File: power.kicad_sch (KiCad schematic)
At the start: 53 parts, among them J1 TYPE-C-31-M-12, U1 USBLC6-2SC6, U2 TLV62569DBVR, U3 AP22653W6-7, U4 AP22653W6-7, U5 AP22653W6-7, U6 AP22653W6-7

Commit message: fix: apply schematic review findings (VIO 5V at power-up, push-pull BOOT, input bias, CC ESD)
Co-Authored-By: Claude Opus 5.5 <noreply@anthropic.com>
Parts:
- removed U1: USBLC6-2SC6, Package_TO_SOT_SMD:SOT-23-6, symbol Power_Protection:USBLC6-2SC6
- removed U2: TLV62569DBVR, Package_TO_SOT_SMD:SOT-23-5, symbol Regulator_Switching:TLV62569DBV
- removed U3: AP22653W6-7, Package_TO_SOT_SMD:SOT-23-6, symbol OOTY:AP22653W6
- added U1: TPD4E05U06DQAR, Package_SON:USON-10_2.5x1.0mm_P0.5mm, symbol Power_Protection:TPD4E05U06DQA
- added U2: USBLC6-2SC6, Package_TO_SOT_SMD:SOT-23-6, symbol Power_Protection:USBLC6-2SC6
- added U3: TLV62569DBVR, Package_TO_SOT_SMD:SOT-23-5, symbol Regulator_Switching:TLV62569DBV
- added U7: AP22653W6-7, Package_TO_SOT_SMD:SOT-23-6, symbol OOTY:AP22653W6
- C2: value 10uF/25V -> 100nF/50V; footprint Capacitor_SMD:C_0805_2012Metric -> Capacitor_SMD:C_0402_1005Metric; LCSC C15850 -> C307331; MPN CL21A106KAYNNNE -> CL05B104KB54PNC
- C3: value 100nF/50V -> 10uF/10V; footprint Capacitor_SMD:C_0402_1005Metric -> Capacitor_SMD:C_0603_1608Metric; LCSC C307331 -> C19702; MPN CL05B104KB54PNC -> CL10A106KP8NNNC
- C4: value 10uF/10V -> 100nF/50V; footprint Capacitor_SMD:C_0603_1608Metric -> Capacitor_SMD:C_0402_1005Metric; LCSC C19702 -> C307331; MPN CL10A106KP8NNNC -> CL05B104KB54PNC
- C5: value 100nF/50V -> 6.8pF DNP; LCSC C307331 -> (none); MPN CL05B104KB54PNC -> (none); Manufacturer Samsung -> (none); now not fitted; now left out of the parts list
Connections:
- net +3V3: now also C5.1, U7.1 (IN), U7.3 (EN); no longer U5.1 (IN), U6.3 (EN)
- net +5V: now also U5.1 (IN), U5.3 (EN), U3.1 (EN), U3.4 (VIN); no longer C5.1, U4.3 (EN)
- net 3V3_DUT: now also U7.6 (OUT); no longer U6.6 (OUT)
- net 3V3_SW_PRE: now also U6.6 (OUT); no longer U5.6 (OUT)
- net 5V_DUT: now also U5.6 (OUT); no longer U4.6 (OUT)
- net 5V_SW_PRE: now also U4.6 (OUT)
- net CC1: now also U1.1 (D1+)
- net CC2: now also U1.2 (D1-)
- net EN_3V3SW: now also U6.3 (EN); no longer U5.3 (EN)
- net EN_5VSW: now also U4.3 (EN)
- net FAULT_3V3: now also U7.4 (~{FAULT}); no longer U6.4 (~{FAULT})
- net FAULT_3V3SW: now also U6.4 (~{FAULT}); no longer U5.4 (~{FAULT})
- net FAULT_5V: now also U5.4 (~{FAULT}); no longer U4.4 (~{FAULT})
- net FAULT_5VSW: now also U4.4 (~{FAULT})
- net FB_3V3: now also C5.2, U3.5 (FB)
- net GND: now also U1.3 (GND), U1.8 (GND), U2.2 (GND), U3.2 (GND), U7.2 (GND); no longer C5.2
- net ILIM_3V3: now also U7.5 (ILIM); no longer U6.5 (ILIM)
- net ILIM_3V3SW: now also U6.5 (ILIM); no longer U5.5 (ILIM)
- net ILIM_5V: now also U5.5 (ILIM); no longer U4.5 (ILIM)
- net ILIM_5VSW: now also U4.5 (ILIM)
- net SW_3V3: now also U3.3 (SW)
- net USB_DM: now also U2.3 (I/O2), U2.4 (I/O2)
- net USB_DP: now also U2.1 (I/O1), U2.6 (I/O1)
- net VBUS: now also U2.5 (VBUS)
- no-connect marks 2 -> 8

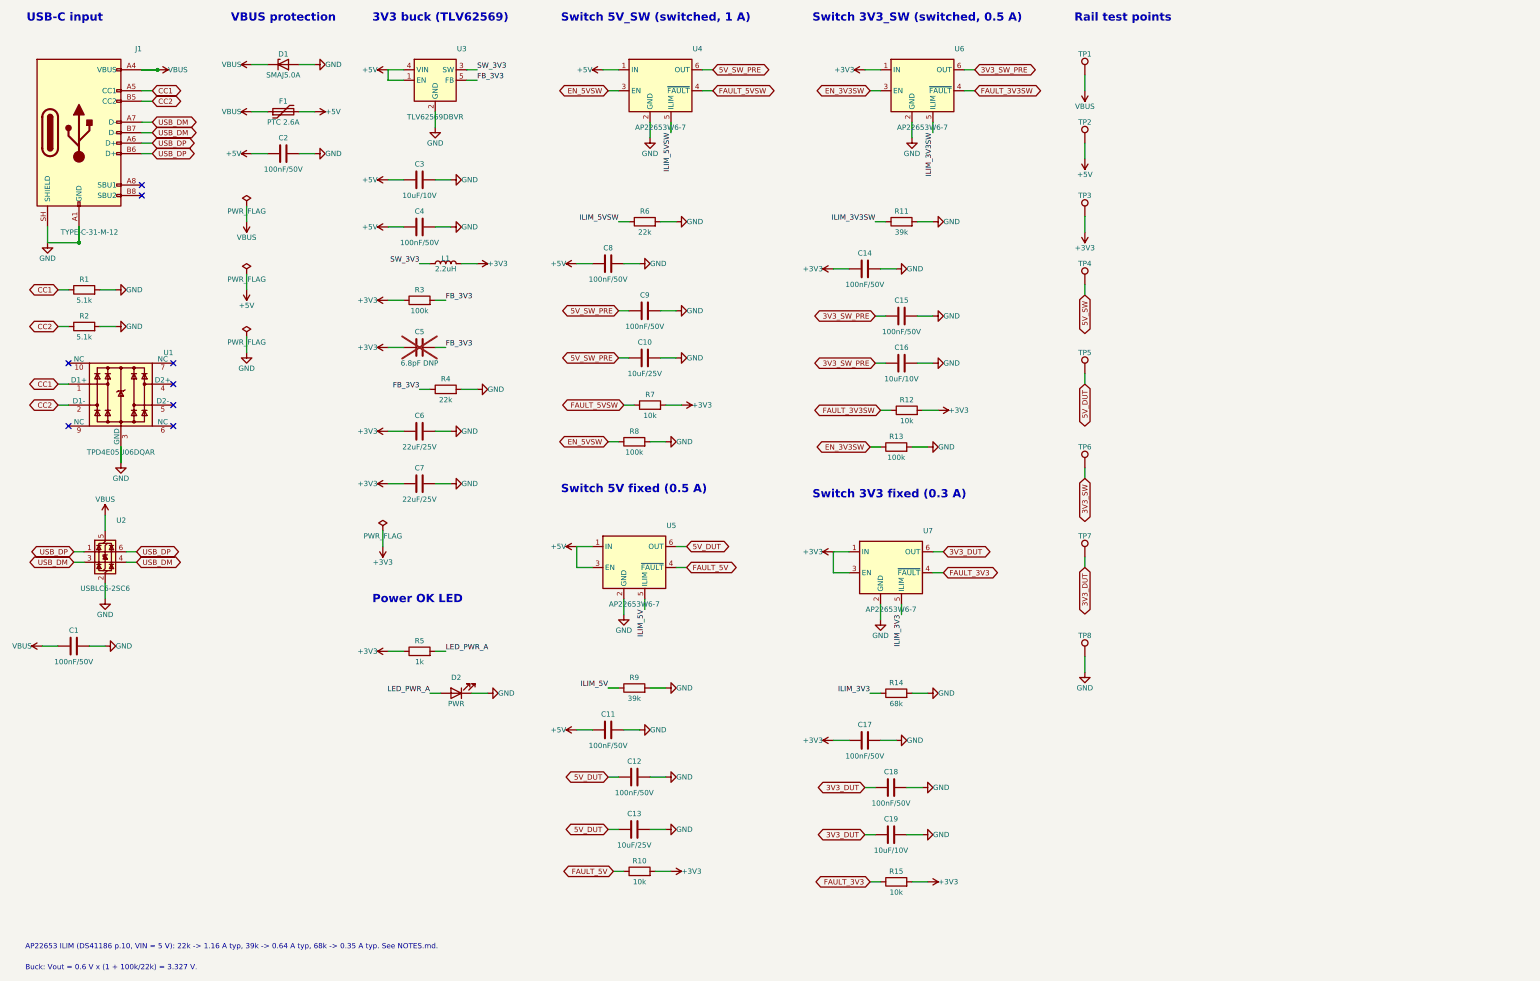
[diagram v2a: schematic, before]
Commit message: fix: apply schematic review (LQFP-80 MCU, fixed-rail EN, VIO from 5V_DUT, buttons, ESD per header)
- STM32G431MBT6 (LQFP-80): 14 more GPIO; BOOT_DIR off PB4 (JTRST pull-up at reset)
- Fixed DUT rails: EN on PE7/PE8 with pull-up (on by default, firmware can cut)
- TPS2116 VIN1 from current-limited 5V_DUT instead of +5V
- Two user push buttons (TS-1187A) on PD0/PD1, BOOT0 solder jumper
- TVS after the PTC, buck Cin 10uF/25V 0805, 5th VDD decoupling cap
- No floating translator inputs (U15 A8 to GND, 1M bias on U14 B side)
- ESD channels grouped per header; datasheet field falls back to LCSC page
- Decoupling capacitors declare the pin they decouple (validated against nets)

Co-Authored-By: Claude Opus 5.5 <noreply@anthropic.com>
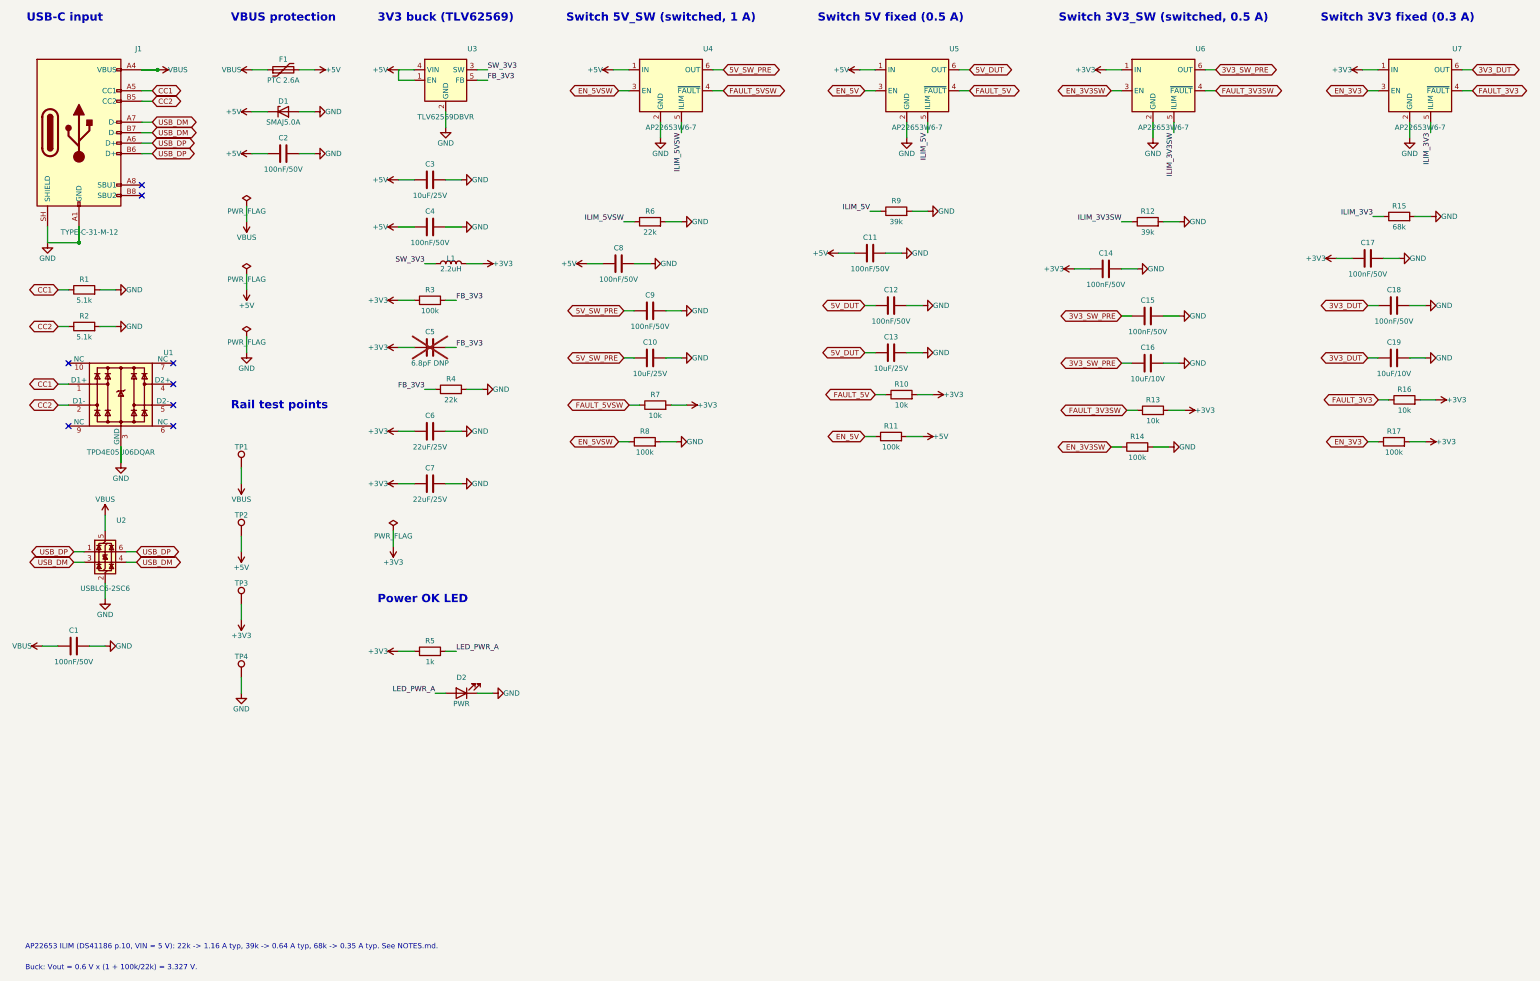
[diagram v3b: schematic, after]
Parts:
- removed TP5: 5V_DUT, TestPoint:TestPoint_Pad_D1.5mm, symbol Connector:TestPoint
- removed TP6: 3V3_SW, TestPoint:TestPoint_Pad_D1.5mm, symbol Connector:TestPoint
- removed TP7: 3V3_DUT, TestPoint:TestPoint_Pad_D1.5mm, symbol Connector:TestPoint
- removed TP8: GND, TestPoint:TestPoint_Pad_D1.5mm, symbol Connector:TestPoint
- added R16: 10k, Resistor_SMD:R_0402_1005Metric, symbol Device:R
- added R17: 100k, Resistor_SMD:R_0402_1005Metric, symbol Device:R
- C3: value 10uF/10V -> 10uF/25V; footprint Capacitor_SMD:C_0603_1608Metric -> Capacitor_SMD:C_0805_2012Metric; LCSC C19702 -> C15850; MPN CL10A106KP8NNNC -> CL21A106KAYNNNE
- R11: value 39k -> 100k; LCSC C25783 -> C25741; MPN 0402WGF3902TCE -> 0402WGF1003TCE
- R12: value 10k -> 39k; LCSC C25744 -> C25783; MPN 0402WGF1002TCE -> 0402WGF3902TCE
- R13: value 100k -> 10k; LCSC C25741 -> C25744; MPN 0402WGF1003TCE -> 0402WGF1002TCE
- R14: value 68k -> 100k; LCSC C36871 -> C25741; MPN 0402WGF6802TCE -> 0402WGF1003TCE
- R15: value 10k -> 68k; LCSC C25744 -> C36871; MPN 0402WGF1002TCE -> 0402WGF6802TCE
- TP4: value 5V_SW -> GND
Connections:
- net 5V_SW is gone; now on net GND: TP4.1
- net +3V3: now also R13.2, R16.2, R17.2; no longer R12.2, R15.2, U7.3 (EN)
- net +5V: now also D1.1 (K), R11.2; no longer U5.3 (EN)
- net EN_3V3SW: now also R14.1; no longer R13.1
- net FAULT_3V3: now also R16.1; no longer R15.1
- net FAULT_3V3SW: now also R13.1; no longer R12.1
- net GND: now also R12.2, R15.2; no longer R11.2, R13.2
- net ILIM_3V3: now also R15.1; no longer R14.1
- net ILIM_3V3SW: now also R12.1; no longer R11.1
- net VBUS: no longer D1.1 (K)
- new net EN_3V3: R17.1, U7.3 (EN)
- new net EN_5V: R11.1, U5.3 (EN)
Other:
- moved on the sheet: C10, C11, C12, C13, C14, C15, C16, C17, C18, C19, C3, C4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

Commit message: fix: apply placement re-review (debug series resistors, USB corridor, shunt orientation, ILIM, EN_5V pull-up to 3V3)
- R83-R87 between the J_DBG drivers and their ESD; keepout corridor for USB D+/D-
- R22/R23 turned so current flows switch -> shunt -> header without crossing
- ILIM resistors next to pin 5 of each AP22653
- EN_5V pull-up to +3V3 instead of +5V (PD8 must not see 5 V while VDD is off)
- Silkscreen: a reference must be within 2 mm of its part and closer to it than to any
  other part (10 key references still without room, to finish with the next placement pass)

DRC with schematic parity: 0 errors. ERC: 0 errors.

Co-Authored-By: Claude Opus 5.5 <noreply@anthropic.com>
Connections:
- net +3V3: now also R11.2
- net +5V: no longer R11.2
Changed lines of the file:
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@@
 	)
 	(symbol
-		(lib_id "power:+5V")
+		(lib_id "power:+3V3")
 		(at 237.49 130.81 270)
 		(unit 1)
@@
 			)
 		)
-		(property "Value" "+5V"
+		(property "Value" "+3V3"
 			(at 240.03 130.81 90)
 			(show_name no)
